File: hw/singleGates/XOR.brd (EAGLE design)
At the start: 15 parts, among them Q1 BC817, Q2 BC817, Q3 BC817, Q4 BC817, Q5 BC817, Q6 BC817

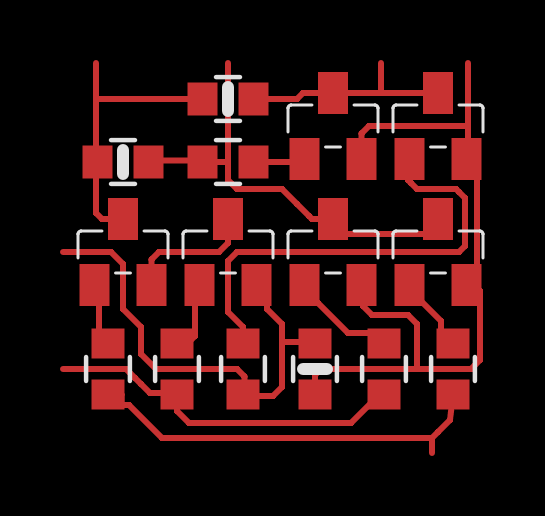
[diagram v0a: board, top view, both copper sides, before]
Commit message: Made components to only have connections on 2 sides
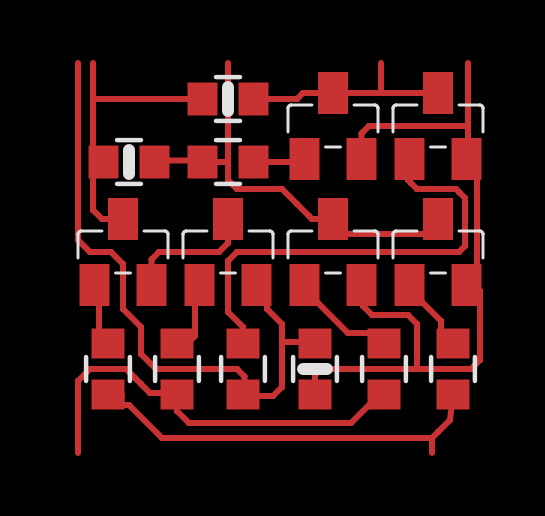
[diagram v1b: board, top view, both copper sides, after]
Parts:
- moved R6 0.20 mm to (2.20, 9.70)
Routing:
- net AND: track 17.3 -> 22.8 mm
- net B: track 12.2 -> 14.2 mm
- net _VP: track 9.60 -> 10.4 mm
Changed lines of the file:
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@@
 <layers>
 <layer number="1" name="Top" color="4" fill="1" visible="yes" active="yes"/>
-<layer number="16" name="Bottom" color="1" fill="1" visible="no" active="yes"/>
+<layer number="16" name="Bottom" color="1" fill="1" visible="yes" active="yes"/>
 <layer number="17" name="Pads" color="2" fill="1" visible="yes" active="yes"/>
 <layer number="18" name="Vias" color="2" fill="1" visible="yes" active="yes"/>
@@
 <layer number="20" name="Dimension" color="15" fill="1" visible="yes" active="yes"/>
 <layer number="21" name="tPlace" color="7" fill="1" visible="yes" active="yes"/>
-<layer number="22" name="bPlace" color="7" fill="1" visible="no" active="yes"/>
+<layer number="22" name="bPlace" color="7" fill="1" visible="yes" active="yes"/>
 <layer number="23" name="tOrigins" color="15" fill="1" visible="yes" active="yes"/>
-<layer number="24" name="bOrigins" color="15" fill="1" visible="no" active="yes"/>
-<layer number="25" name="tNames" color="7" fill="1" visible="no" active="yes"/>
-<layer number="26" name="bNames" color="7" fill="1" visible="no" active="yes"/>
-<layer number="27" name="tValues" color="7" fill="1" visible="no" active="yes"/>
-<layer number="28" name="bValues" color="7" fill="1" visible="no" active="yes"/>
+<layer number="24" name="bOrigins" color="15" fill="1" visible="yes" active="yes"/>
+<layer number="25" name="tNames" color="7" fill="1" visible="yes" active="yes"/>
+<layer number="26" name="bNames" color="7" fill="1" visible="yes" active="yes"/>
+<layer number="27" name="tValues" color="7" fill="1" visible="yes" active="yes"/>
+<layer number="28" name="bValues" color="7" fill="1" visible="yes" active="yes"/>
 <layer number="29" name="tStop" color="7" fill="3" visible="no" active="yes"/>
 <layer number="30" name="bStop" color="7" fill="6" visible="no" active="yes"/>
@@
 <layer number="38" name="bTest" color="7" fill="1" visible="no" active="yes"/>
 <layer number="39" name="tKeepout" color="4" fill="11" visible="yes" active="yes"/>
-<layer number="40" name="bKeepout" color="1" fill="11" visible="no" active="yes"/>
+<layer number="40" name="bKeepout" color="1" fill="11" visible="yes" active="yes"/>
 <layer number="41" name="tRestrict" color="4" fill="10" visible="yes" active="yes"/>
-<layer number="42" name="bRestrict" color="1" fill="10" visible="no" active="yes"/>
-<layer number="43" name="vRestrict" color="2" fill="10" visible="no" active="yes"/>
+<layer number="42" name="bRestrict" color="1" fill="10" visible="yes" active="yes"/>
+<layer number="43" name="vRestrict" color="2" fill="10" visible="yes" active="yes"/>
 <layer number="44" name="Drills" color="7" fill="1" visible="no" active="yes"/>
 <layer number="45" name="Holes" color="7" fill="1" visible="no" active="yes"/>
 <layer number="46" name="Milling" color="3" fill="1" visible="no" active="yes"/>
 <layer number="47" name="Measures" color="7" fill="1" visible="no" active="yes"/>
-<layer number="48" name="Document" color="7" fill="1" visible="no" active="yes"/>
-<layer number="49" name="Reference" color="7" fill="1" visible="no" active="yes"/>
+<layer number="48" name="Document" color="7" fill="1" visible="yes" active="yes"/>
+<layer number="49" name="Reference" color="7" fill="1" visible="yes" active="yes"/>
 <layer number="50" name="dxf" color="7" fill="1" visible="no" active="no"/>
 <layer number="51" name="tDocu" color="7" fill="1" visible="yes" active="yes"/>
-<layer number="52" name="bDocu" color="7" fill="1" visible="no" active="yes"/>
+<layer number="52" name="bDocu" color="7" fill="1" visible="yes" active="yes"/>
 <layer number="53" name="tGND_GNDA" color="7" fill="9" visible="no" active="no"/>
 <layer number="54" name="bGND_GNDA" color="1" fill="9" visible="no" active="no"/>
@@
 <wire x1="0" y1="13" x2="0" y2="0" width="0.2" layer="22" style="shortdash"/>
 <wire x1="5.5" y1="12.2" x2="5.5" y2="11.4" width="0.4" layer="21"/>
-<wire x1="2" y1="10.1" x2="2" y2="9.3" width="0.4" layer="21"/>
+<wire x1="2.2" y1="9.3" x2="2.2" y2="10.1" width="0.4" layer="21"/>
 <wire x1="8" y1="2.8" x2="8.8" y2="2.8" width="0.4" layer="21"/>
 </plain>
@@
 <attribute name="SV_SPICE_PREFIX" value="R" x="8.4" y="2.8" size="1.778" layer="27" rot="R90" display="off"/>
 </element>
-<element name="R6" library="p.peter-gator" package="R0603" value="1k" x="2" y="9.7" smashed="yes" rot="R180">
-<attribute name="SV_SPICE_ORDER" value="1;2" x="2" y="9.7" size="1.778" layer="27" rot="R180" display="off"/>
-<attribute name="SV_SPICE_PREFIX" value="R" x="2" y="9.7" size="1.778" layer="27" rot="R180" display="off"/>
+<element name="R6" library="p.peter-gator" package="R0603" value="1k" x="2.2" y="9.7" smashed="yes" rot="R180">
+<attribute name="SV_SPICE_ORDER" value="1;2" x="2.2" y="9.7" size="1.778" layer="27" rot="R180" display="off"/>
+<attribute name="SV_SPICE_PREFIX" value="R" x="2.2" y="9.7" size="1.778" layer="27" rot="R180" display="off"/>
 </element>
 <element name="R9" library="p.peter-gator" package="R0603" value="1k" x="5.5" y="11.8" smashed="yes" rot="R180">
@@
 <signal name="_VP">
 <contactref element="R9" pad="2"/>
-<wire x1="1.1" y1="9.7" x2="1.1" y2="11" width="0.2" layer="1"/>
 <wire x1="2" y1="7.8" x2="1.3" y2="7.8" width="0.2" layer="1"/>
-<wire x1="1.3" y1="7.8" x2="1.1" y2="8" width="0.2" layer="1"/>
-<wire x1="1.1" y1="8" x2="1.1" y2="9.65" width="0.2" layer="1"/>
-<wire x1="1.1" y1="11" x2="1.1" y2="11.4" width="0.2" layer="1"/>
+<wire x1="1.3" y1="7.8" x2="1" y2="8.1" width="0.2" layer="1"/>
+<wire x1="1" y1="8.1" x2="1" y2="9.75" width="0.2" layer="1"/>
+<wire x1="1.1" y1="9.7" x2="1" y2="9.7" width="0.2" layer="1"/>
 <wire x1="1.5" y1="11.8" x2="4.65" y2="11.8" width="0.2" layer="1"/>
-<wire x1="1.1" y1="11.4" x2="1.1" y2="11.8" width="0.2" layer="1"/>
-<wire x1="1.1" y1="11.8" x2="1.1" y2="13" width="0.2" layer="1"/>
-<wire x1="1.5" y1="11.8" x2="1.1" y2="11.8" width="0.2" layer="1"/>
+<wire x1="1" y1="9.7" x2="1" y2="9.75" width="0.2" layer="1"/>
+<wire x1="1" y1="9.75" x2="1" y2="11.8" width="0.2" layer="1"/>
+<wire x1="1" y1="11.8" x2="1" y2="13" width="0.2" layer="1"/>
+<wire x1="1.5" y1="11.8" x2="1" y2="11.8" width="0.2" layer="1"/>
 <contactref element="R6" pad="2"/>
 <contactref element="Q1" pad="P$3"/>
-<wire x1="1.1" y1="9.65" x2="1.15" y2="9.7" width="0.2" layer="1"/>
-<wire x1="1.1" y1="9.7" x2="1.15" y2="9.7" width="0.2" layer="1"/>
+<wire x1="1" y1="9.75" x2="1.35" y2="9.7" width="0.2" layer="1"/>
+<wire x1="1.1" y1="9.7" x2="1.35" y2="9.7" width="0.2" layer="1"/>
 </signal>
 <signal name="N$19">
@@
 <contactref element="R7" pad="1"/>
 <wire x1="5.5" y1="9.7" x2="5.5" y2="10.7" width="0.2" layer="1"/>
-<wire x1="2.9" y1="9.75" x2="2.85" y2="9.7" width="0.2" layer="1"/>
+<wire x1="2.9" y1="9.75" x2="3.05" y2="9.7" width="0.2" layer="1"/>
 <wire x1="4.65" y1="9.7" x2="5.5" y2="9.7" width="0.2" layer="1"/>
 <wire x1="2.9" y1="9.75" x2="4.6" y2="9.75" width="0.2" layer="1"/>
@@
 <wire x1="10.5" y1="1.9" x2="10.65" y2="1.9" width="0.2" layer="1"/>
 <wire x1="10.65" y1="1.9" x2="10.7" y2="1.95" width="0.2" layer="1"/>
-<wire x1="0.9" y1="2.8" x2="0" y2="2.8" width="0.2" layer="1"/>
+<wire x1="0.9" y1="2.8" x2="0.5" y2="2.4" width="0.2" layer="1"/>
+<wire x1="0.5" y1="2.4" x2="0.5" y2="0" width="0.2" layer="1"/>
 <wire x1="0.9" y1="2.8" x2="2.1" y2="2.8" width="0.2" layer="1"/>
 <wire x1="2.1" y1="2.8" x2="2.4" y2="2.5" width="0.2" layer="1"/>
@@
 <wire x1="2" y1="4.8" x2="2" y2="6.3" width="0.2" layer="1"/>
 <wire x1="2" y1="6.3" x2="1.6" y2="6.7" width="0.2" layer="1"/>
-<wire x1="1.6" y1="6.7" x2="0" y2="6.7" width="0.2" layer="1"/>
+<wire x1="1.6" y1="6.7" x2="0.9" y2="6.7" width="0.2" layer="1"/>
+<wire x1="0.9" y1="6.7" x2="0.5" y2="7.1" width="0.2" layer="1"/>
+<wire x1="0.5" y1="7.1" x2="0.5" y2="13" width="0.2" layer="1"/>
 <wire x1="6" y1="1.95" x2="6" y2="2.05" width="0.2" layer="1"/>
 <wire x1="6" y1="2.05" x2="6.05" y2="2.1" width="0.2" layer="1"/>

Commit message: Trying to mimize gates some more
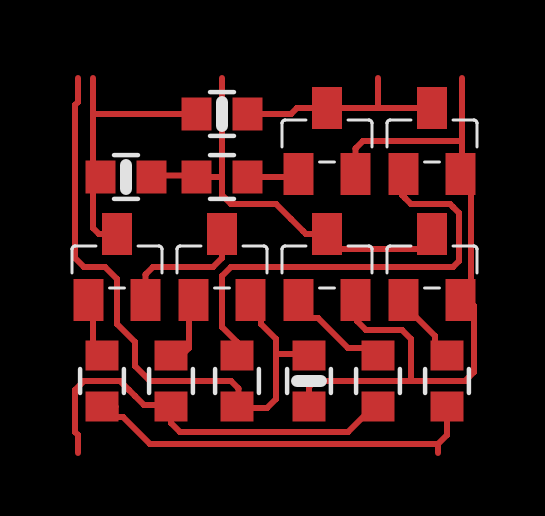
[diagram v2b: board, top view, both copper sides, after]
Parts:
- moved Q2 0.54 mm to (5.30, 6.20)
- moved R7 0.54 mm to (5.30, 9.20)
- moved R9 0.54 mm to (5.30, 11.3)
- moved Q1 0.54 mm to (1.80, 6.20)
- moved Q3 0.54 mm to (8.80, 6.20)
- moved Q4 0.54 mm to (12.3, 6.20)
- moved Q5 0.54 mm to (8.80, 10.4)
- moved Q6 0.54 mm to (12.3, 10.4)
- moved R6 0.51 mm to (2.10, 9.20)
- moved R3 0.45 mm to (8.20, 2.40)
- moved R8 0.45 mm to (5.80, 2.40)
- moved R1 0.45 mm to (1.30, 2.40)
- moved R2 0.45 mm to (3.60, 2.40)
- moved R4 0.45 mm to (12.8, 2.40)
- moved R5 0.45 mm to (10.5, 2.40)
